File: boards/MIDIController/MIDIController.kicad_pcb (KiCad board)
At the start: 2 copper layers, 150 x 100 mm, 31 parts, among them J1 Ctrl, J2 MIDICon, J3 IO_Boards, J4 USB_A, J5 I2S_Data, J6 I2C_Pwr, J7 Raspberry_Pi_2_3, J8 RJ45_Amphenol_RJMG1BD3B8K1ANR, U1 Teensy4.1

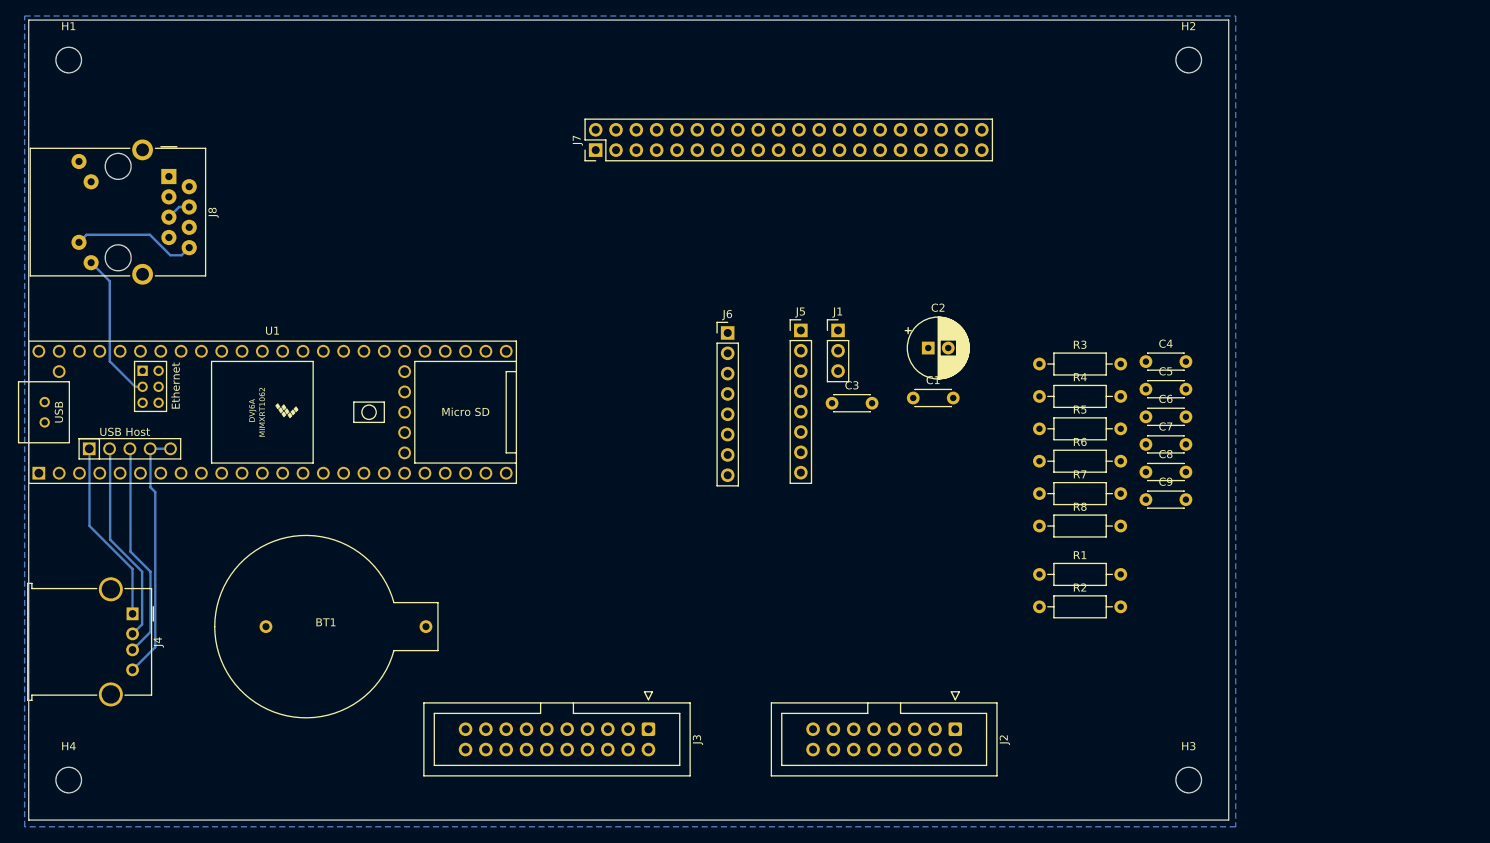
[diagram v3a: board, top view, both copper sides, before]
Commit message: Updated design rules to 0.32mm template and exported Gerber files
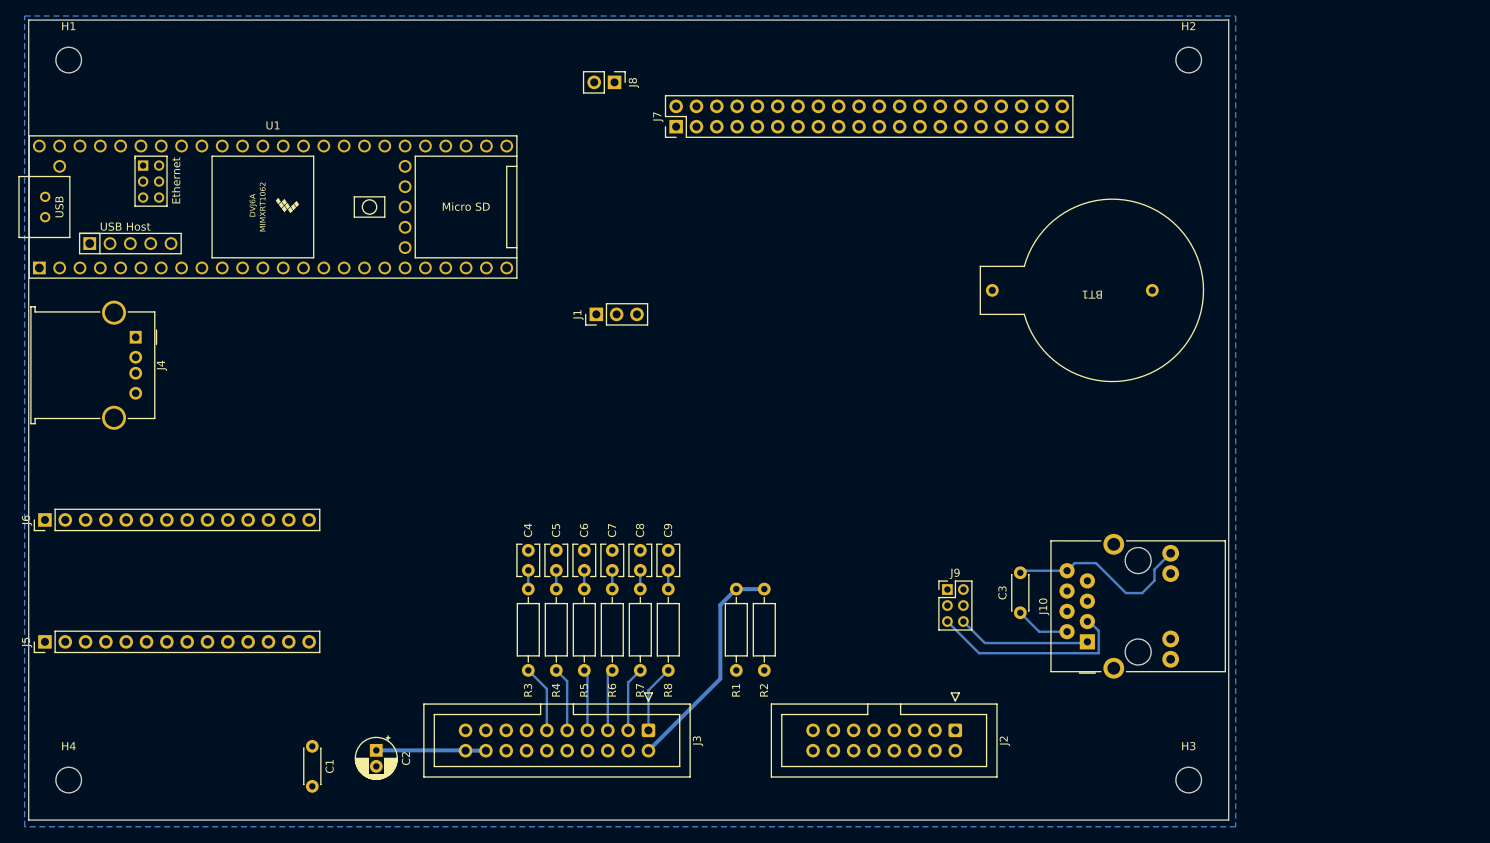
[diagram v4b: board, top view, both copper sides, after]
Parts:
- added J10: RJ45_Bel_SI-60062-F_fixed, Connector_RJ:RJ45_Bel_SI-60062-F, F.Cu at (198.9, 122.9)
- added J9: Eth, Connector_PinHeader_2.00mm:PinHeader_2x03_P2.00mm_Vertical, F.Cu at (181.4, 116.4)
- C2: footprint Capacitor_THT:CP_Radial_D7.5mm_P2.50mm -> Capacitor_THT:CP_Radial_D5.0mm_P2.00mm
- C4, C5, C6, C7, C8, C9: footprint Capacitor_THT:C_Disc_D4.3mm_W1.9mm_P5.00mm -> Capacitor_THT:C_Disc_D3.8mm_W2.6mm_P2.50mm
- J5: value I2S_Data -> I2S1; footprint Connector_PinHeader_2.54mm:PinHeader_1x08_P2.54mm_Vertical -> Connector_PinHeader_2.54mm:PinHeader_1x14_P2.54mm_Vertical
- J6: value I2C_Pwr -> I2S2; footprint Connector_PinHeader_2.54mm:PinHeader_1x08_P2.54mm_Vertical -> Connector_PinHeader_2.54mm:PinHeader_1x14_P2.54mm_Vertical
- J8: value RJ45_Amphenol_RJMG1BD3B8K1ANR -> RPI_Pwr; footprint Connector_RJ:RJ45_Amphenol_RJMG1BD3B8K1ANR -> Connector_PinHeader_2.54mm:PinHeader_1x02_P2.54mm_Vertical
- U1: footprint Teensy:Teensy41 -> teensy:Teensy41
- moved BT1 104.6 mm to (199.5, 79.0), turned to 180 degrees
- moved J5 102.2 mm to (68.6, 122.9), turned to 90 degrees
- moved J6 88.5 mm to (68.6, 107.7), turned to 90 degrees
- moved C1 86.8 mm to (102.0, 136.0), turned to -90 degrees
- moved C2 85.4 mm to (110.0, 136.5), turned to -90 degrees
- moved C4 81.5 mm to (129.0, 114.0), turned to 90 degrees
- moved C5 77.1 mm to (132.5, 114.0), turned to 90 degrees
- moved C6 72.8 mm to (136.0, 114.0), turned to 90 degrees
- moved R3 69.8 mm to (129.0, 116.3), turned to -90 degrees
- moved C7 68.5 mm to (139.5, 114.0), turned to 90 degrees
- moved R4 65.0 mm to (132.5, 116.3), turned to -90 degrees
- moved C8 64.4 mm to (143.0, 114.0), turned to 90 degrees
- moved C9 60.4 mm to (146.5, 114.0), turned to 90 degrees
- moved R5 60.3 mm to (136.0, 116.3), turned to -90 degrees
- moved J8 56.9 mm to (139.8, 53.0)
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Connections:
- C3 pad 1: Net-(J8-RCT) -> Net-(J10-RCT)
- J4 pad 5: unconnected-(J4-Shield-Pad5) -> GND
- J5 pad 1: /SCL -> GND
- J5 pad 2: /SDA -> unconnected-(J5-Pin_2-Pad2)
- J5 pad 3: /I2S_MCLK2 -> unconnected-(J5-Pin_3-Pad3)
- J5 pad 4: /I2S_OUT2 -> unconnected-(J5-Pin_4-Pad4)
- J5 pad 5: /I2S_LRCLK2 -> unconnected-(J5-Pin_5-Pad5)
- J5 pad 6: /I2S_BCLK2 -> unconnected-(J5-Pin_6-Pad6)
- J5 pad 7: /I2S_IN2 -> unconnected-(J5-Pin_7-Pad7)
- J5 pad 8: GND -> /I2S_MEMCS
- J6 pad 1: +5V -> unconnected-(J6-Pin_1-Pad1)
- J6 pad 2: +5V -> GND
- J6 pad 4: +3.3V -> /I2S_MCLK2
- J6 pad 6: /SPDIF_OUT -> /I2S_BCLK2
- J6 pad 7: GND -> /I2S_LRCLK2
- J6 pad 8: GND -> /SCL
- J7 pad 2: +5V -> Net-(J8-Pin_2)
- J7 pad 4: +5V -> Net-(J8-Pin_2)
- J7 pad 7: unconnected-(J7-GCLK0/GPIO4-Pad7) -> /Int_RPI
- U1 pad 12: /RPI_CS -> /I2S_CS
- U1 pad 13: /RPI_MOSI -> /I2S_MOSI
- U1 pad 14: /RPI_MISO -> /I2S_MISO
- U1 pad 18: unconnected-(U1-26_A12_MOSI1-Pad18) -> /RPI_MOSI
- U1 pad 19: unconnected-(U1-27_A13_SCK1-Pad19) -> /RPI_SCLK
- U1 pad 22: unconnected-(U1-30_CRX3-Pad22) -> /Int_StopRight
- U1 pad 23: unconnected-(U1-31_CTX3-Pad23) -> /Int_StopLeft
- U1 pad 27: unconnected-(U1-35_TX8-Pad27) -> /Int_RPI
- U1 pad 30: /Int_StopLeft -> /RPI_CS
- U1 pad 31: /Int_StopRight -> /RPI_MISO
- U1 pad 35: /RPI_SCLK -> /I2S_SCLK
- U1 pad 44: unconnected-(U1-22_A8_CTX1-Pad44) -> /VOL_A8
- U1 pad 46: +3.3V -> unconnected-(U1-3V3-Pad46)
- U1 pad 60: /Eth_R+ -> unconnected-(U1-R+-Pad60)
- U1 pad 61: /Eth_LED -> unconnected-(U1-LED-Pad61)
- U1 pad 62: /Eth_T- -> unconnected-(U1-T--Pad62)
- U1 pad 63: /Eth_T+ -> unconnected-(U1-T+-Pad63)
- U1 pad 64: /Eth_Gnd -> unconnected-(U1-GND-Pad64)
- U1 pad 65: /Eth_R- -> unconnected-(U1-R--Pad65)
- U1 pad 8: unconnected-(U1-6_OUT1D-Pad8) -> /I2S_MEMCS
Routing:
- net Net-(J4-GND): track 31.6 -> 0.00 mm
- net +3.3V: track 0.00 -> 28.2 mm
- net Net-(J4-D+): track 27.1 -> 0.00 mm
- net Net-(J4-D-): track 25.3 -> 0.00 mm
- net /Eth_T-: track 0.00 -> 25.3 mm
- net Net-(J4-VBUS): track 22.9 -> 0.00 mm
- net /Eth_LED: track 18.7 -> 0.00 mm
- net /Eth_T+: track 0.00 -> 16.7 mm
- net +5V: track 0.00 -> 13.7 mm
- net Net-(J3-Pin_1): track 0.00 -> 8.53 mm
- net Net-(J3-Pin_11): track 0.00 -> 8.46 mm
- net Net-(J3-Pin_3): track 0.00 -> 8.13 mm
- net /Eth_Gnd: track 15.6 -> 23.7 mm
- net Net-(J3-Pin_9): track 0.00 -> 8.06 mm
- net Net-(J3-Pin_5): track 0.00 -> 7.73 mm
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
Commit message: Fixed some RX/TX pin swaps
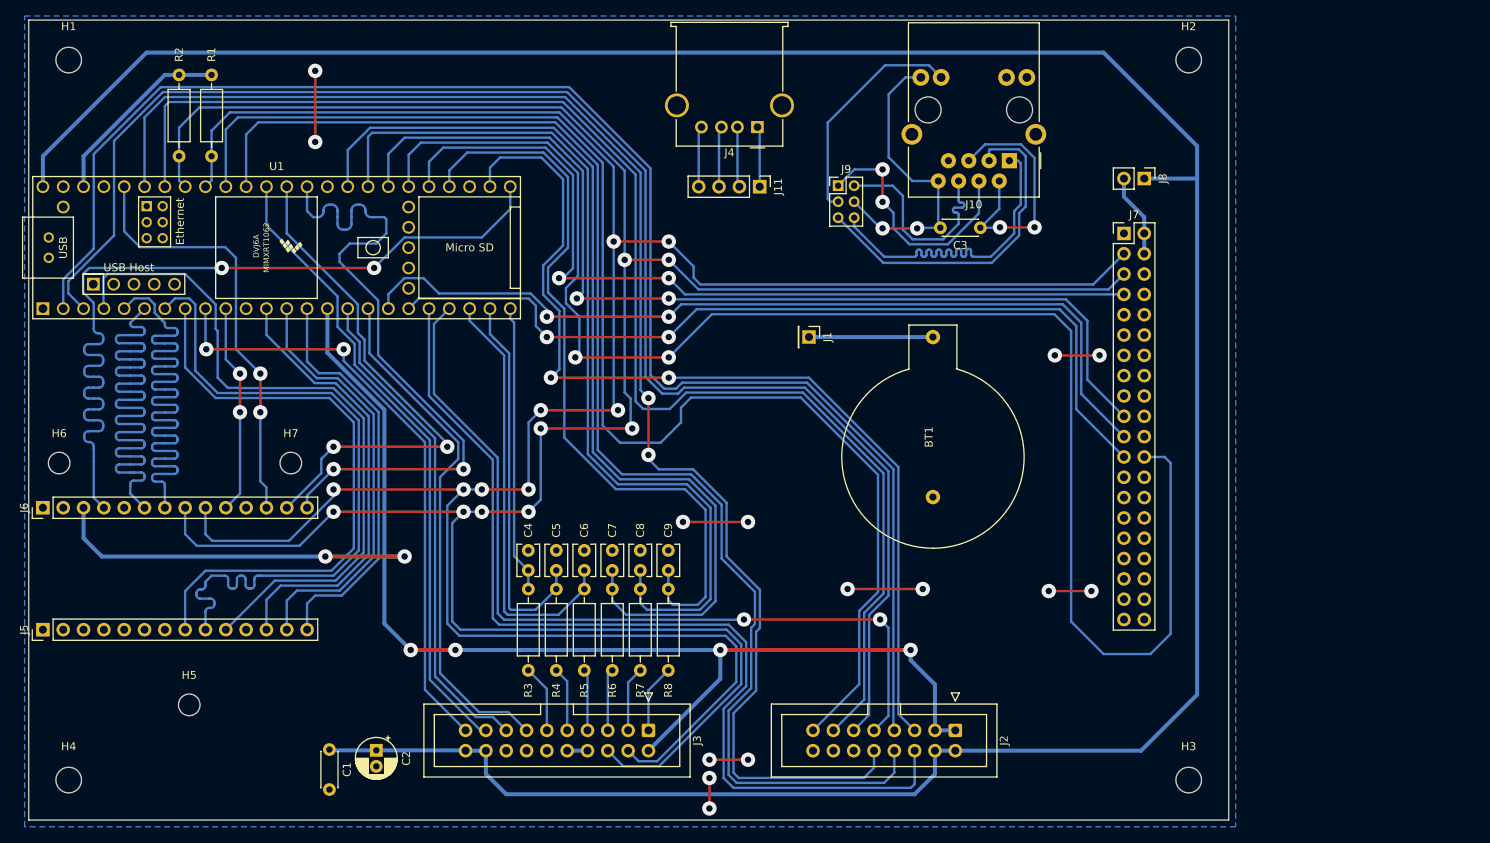
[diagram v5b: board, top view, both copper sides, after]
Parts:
- added H5: MountingHole, MountingHole:MountingHole_2.7mm_M2.5, F.Cu at (86.6, 130.8)
- added H6: MountingHole, MountingHole:MountingHole_2.7mm_M2.5, F.Cu at (70.4, 100.6)
- added H7: MountingHole, MountingHole:MountingHole_2.7mm_M2.5, F.Cu at (99.3, 100.6)
- added J11: USB, Connector_PinHeader_2.54mm:PinHeader_1x04_P2.54mm_Vertical, F.Cu at (157.9, 66.0)
- J1: value Ctrl -> VBAT; footprint Connector_PinHeader_2.54mm:PinHeader_1x03_P2.54mm_Vertical -> Connector_PinHeader_2.54mm:PinHeader_1x01_P2.54mm_Vertical
- moved R2 97.4 mm to (85.3, 62.2)
- moved R1 91.8 mm to (89.4, 62.2)
- moved J4 82.0 mm to (157.6, 58.6), turned to 180 degrees
- moved J8 67.3 mm to (206.0, 65.0)
- moved J10 60.9 mm to (189.1, 62.8), turned to 180 degrees
- moved J7 57.5 mm to (203.5, 71.9), turned to 0 degrees
- moved J9 52.3 mm to (167.7, 65.9)
- moved C3 48.4 mm to (185.5, 71.2), turned to 180 degrees
- moved BT1 27.1 mm to (179.6, 97.3), turned to 90 degrees
- moved J1 26.7 mm to (164.1, 84.8), turned to -90 degrees
- moved U1 5.10 mm to (97.5, 73.7)
- moved C1 2.18 mm to (104.1, 136.4)
- moved J5 1.55 mm to (68.3, 121.4)
- moved J6 1.55 mm to (68.3, 106.2)
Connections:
- J1 pad 1: Net-(J1-Pin_1) -> Net-(BT1-+)
- J2 pad 10: /RXD6 -> /RXD5
- J2 pad 11: /TXD2 -> /TXD1
- J2 pad 13: /TXD6 -> /TXD5
- J2 pad 15: /TXD7 -> /TXD4
- J2 pad 6: /RXD1 -> /RXD7
- J2 pad 7: /RXD2 -> /RXD1
- J2 pad 8: /RXD7 -> /RXD4
- J2 pad 9: /TXD1 -> /TXD7
- J3 pad 13: /TXD5 -> /RXD6
- J3 pad 15: /RXD5 -> /TXD6
- J3 pad 17: /RXD4 -> /RXD3
- J3 pad 19: /RXD3 -> /RXD2
- J4 pad 1: Net-(J4-VBUS) -> Net-(J11-Pin_1)
- J4 pad 2: Net-(J4-D-) -> Net-(J11-Pin_2)
- J4 pad 3: Net-(J4-D+) -> Net-(J11-Pin_3)
- J4 pad 4: Net-(J4-GND) -> Net-(J11-Pin_4)
- J6 pad 10: /TXD4 -> /TXD2
- R1 pad 2: +3.3V -> +3.3V'
- R2 pad 2: +3.3V -> +3.3V'
- U1 pad 22: /Int_StopRight -> /Int_ToeStud
- U1 pad 23: /Int_StopLeft -> /Int_Technics
- U1 pad 24: unconnected-(U1-32_OUT1B-Pad24) -> /Int_Kbd
- U1 pad 27: /Int_RPI -> unconnected-(U1-35_TX8-Pad27)
- U1 pad 29: /Int_ToeStud -> /Int_RPI
- U1 pad 32: /Int_Technics -> /Int_StopLeft
- U1 pad 33: /Int_Kbd -> /Int_StopRight
- U1 pad 46: unconnected-(U1-3V3-Pad46) -> +3.3V'
- U1 pad 50: Net-(BT1-+) -> unconnected-(U1-VBAT-Pad50)
- U1 pad 52: Net-(J1-Pin_3) -> unconnected-(U1-GND-Pad52)
- U1 pad 53: Net-(J1-Pin_2) -> unconnected-(U1-PROGRAM-Pad53)
- U1 pad 54: Net-(J1-Pin_1) -> unconnected-(U1-ON_OFF-Pad54)
- U1 pad 55: Net-(J4-VBUS) -> unconnected-(U1-5V-Pad55)
- U1 pad 56: Net-(J4-D-) -> unconnected-(U1-D--Pad56)
- U1 pad 57: Net-(J4-D+) -> unconnected-(U1-D+-Pad57)
- U1 pad 58: Net-(J4-GND) -> unconnected-(U1-GND-Pad58)
- U1 pad 59: Net-(J4-GND) -> unconnected-(U1-GND-Pad59)
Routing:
- net +5V: track 13.7 -> 352.6 mm
- net /SCL: track 0.00 -> 314.4 mm, vias 0 -> 8
- net /SDA: track 0.00 -> 305.3 mm, vias 0 -> 8
- net /RPI_CS: track 0.00 -> 193.4 mm, vias 0 -> 2
- net /TXD1: track 0.00 -> 193.0 mm
- net /RXD1: track 0.00 -> 192.4 mm
- net /RXD5: track 0.00 -> 181.2 mm, vias 0 -> 2
- net /TXD5: track 0.00 -> 172.4 mm
- net /RXD4: track 0.00 -> 168.5 mm
- net /TXD4: track 0.00 -> 168.1 mm
- net +3.3V: track 28.2 -> 187.0 mm, vias 0 -> 6
- net /RPI_MISO: track 0.00 -> 126.0 mm, vias 0 -> 2
- net /RXD8: track 0.00 -> 122.1 mm, vias 0 -> 2
- net /RXD7: track 0.00 -> 121.8 mm
- net /Int_StopRight: track 2.34 -> 122.2 mm
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
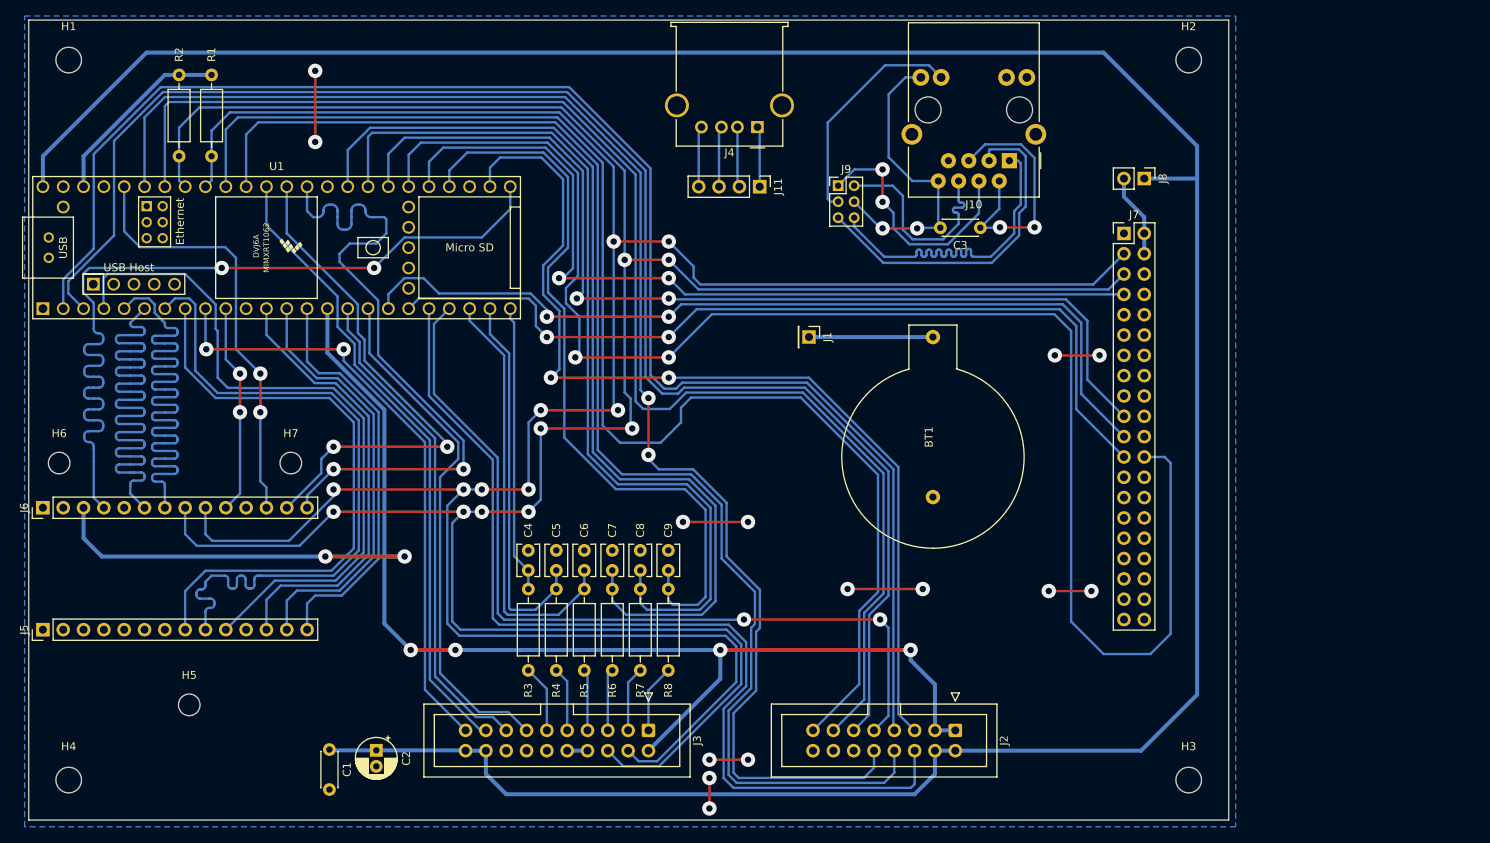
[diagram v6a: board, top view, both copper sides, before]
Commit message: Fixed mirrored MIDI board connector
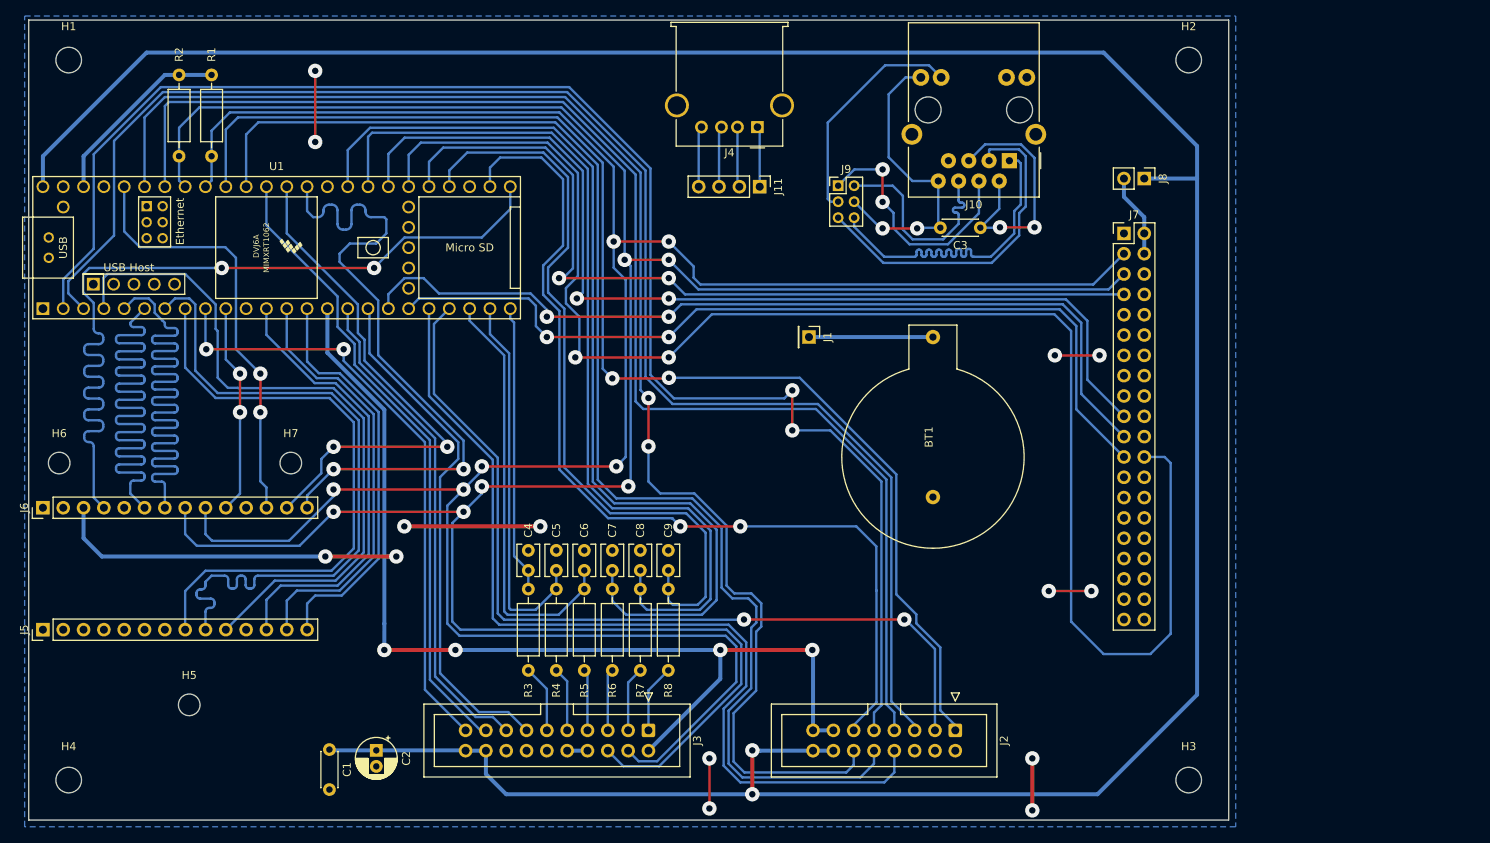
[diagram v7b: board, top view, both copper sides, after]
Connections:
- J2 pad 1: +3.3V -> /TXD4
- J2 pad 10: /RXD5 -> /RXD4
- J2 pad 11: /TXD1 -> /RXD8
- J2 pad 12: GND -> /RXD5
- J2 pad 13: /TXD5 -> +3.3V
- J2 pad 14: GND -> +5V
- J2 pad 15: /TXD4 -> +3.3V
- J2 pad 16: GND -> +5V
- J2 pad 2: +5V -> GND
- J2 pad 3: +3.3V -> /TXD7
- J2 pad 4: +5V -> GND
- J2 pad 5: /RXD8 -> /TXD1
- J2 pad 6: /RXD7 -> GND
- J2 pad 7: /RXD1 -> /TXD5
- J2 pad 8: /RXD4 -> /RXD7
- J2 pad 9: /TXD7 -> /RXD1
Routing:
- net +5V: track 352.6 -> 366.5 mm, vias 0 -> 2
- net +3.3V: track 187.0 -> 173.4 mm
- net /TXD4: track 168.1 -> 159.6 mm, vias 0 -> 2
- net /RXD7: track 121.8 -> 117.0 mm
- net /TXD5: track 172.4 -> 168.4 mm
- net /RXD8: track 122.1 -> 118.5 mm
- net GND: track 46.0 -> 49.6 mm, vias 14 -> 12
- net /TXD7: track 105.4 -> 108.9 mm
- net /RXD4: track 168.5 -> 165.8 mm
- net /RXD5: track 181.2 -> 178.4 mm
- net /TXD1: track 193.0 -> 191.7 mm
- net /RXD1: track 192.4 -> 193.6 mm, vias 0 -> 2
- net /SCL: track 314.4 -> 313.6 mm, vias 8 -> 6
- net /Int_StopRight: track 122.2 -> 122.9 mm
- net /Int_StopLeft: track 114.8 -> 115.3 mm
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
